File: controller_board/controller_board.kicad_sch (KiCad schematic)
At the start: 51 parts, among them IC1 LD1117-3.3V-SOT223, J3 DebugUSART (PinHeader_01x03_P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, J4 Debug GPIO (PinHeader_01x02_P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, Q1 DTC114ECA (SOT-23), Q2 DTC114ECA (SOT-23), U1 ADM3485EARZ-REEL (SOIC-8), U2 PAI141M30 (SOIC-16), U5 SMU02N-05

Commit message: DC, contr, mb, step v2
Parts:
- removed J3: DebugUSART (PinHeader_01x03_P2.54mm), Connector_PinHeader_2.54mm:PinHeader_1x03_P2.54mm_Vertical, symbol Connector:Conn_01x03_Pin
- removed J4: Debug GPIO (PinHeader_01x02_P2.54mm), Connector_PinHeader_2.54mm:PinHeader_1x02_P2.54mm_Vertical, symbol Connector:Conn_01x02_Pin
- C13, C5, C8, C9: value 0,1uF 50V 0805 -> 0,1uF 100V 0603; footprint PCM_Capacitor_SMD_AKL:C_0805_2012Metric_Pad1.18x1.45mm_HandSolder -> Capacitor_SMD:C_0603_1608Metric
- C14: value 47uF 63V D10,5 -> 47uF 63V D6,3 H11
- C2, C7: value 270 pf X7R 1206 2000v 202R18W271KW4E -> 270 pf X7R 1206 2000v 202R18W271KW4E
- IC1: footprint PCM_Package_TO_SOT_SMD_AKL:SOT-89-3_BigPads -> PCM_Package_TO_SOT_SMD_AKL:SOT-223-3_TabPin2
- U2: value PAI141M30 (SOIC-16) -> pia141M30 (SOIC-16)
- renumbered TP26 to TP1, TP27 to TP1, TP28 to TP1, TP29 to TP1, TP30 to TP1, TP32 to TP1, TP33 to TP1, TP31 to TP1, TP25 to TP1
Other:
- sheet NUCLEO-64F411 ports: added none; removed DE_USART6, GPIO1, GPIO2, RX_USART6, TX_USART6

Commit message: DC, contr, mb, digit in v2.1
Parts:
- C12: footprint PCM_Capacitor_SMD_AKL:C_0805_2012Metric_Pad1.18x1.45mm_HandSolder -> Capacitor_SMD:C_0805_2012Metric

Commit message: controller метализированные отверстия
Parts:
- H3, H4, H5: footprint MountingHole:MountingHole_3.2mm_M3 -> MountingHole:MountingHole_3.2mm_M3_DIN965_Pad
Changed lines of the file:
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@@
       (effects (font (size 1.27 1.27)) (justify left) hide)
     )
-    (property "Footprint" "MountingHole:MountingHole_3.2mm_M3" (at 137.16 185.42 0)
+    (property "Footprint" "MountingHole:MountingHole_3.2mm_M3_DIN965_Pad" (at 137.16 185.42 0)
       (effects (font (size 1.27 1.27)) hide)
     )
@@
       (effects (font (size 1.27 1.27)) (justify left) hide)
     )
-    (property "Footprint" "MountingHole:MountingHole_3.2mm_M3" (at 118.11 185.42 0)
+    (property "Footprint" "MountingHole:MountingHole_3.2mm_M3_DIN965_Pad" (at 118.11 185.42 0)
       (effects (font (size 1.27 1.27)) hide)
     )
@@
       (effects (font (size 1.27 1.27)) (justify left) hide)
     )
-    (property "Footprint" "MountingHole:MountingHole_3.2mm_M3" (at 95.25 185.42 0)
-      (effects (font (size 1.27 1.27)) hide)
-    )
+    (property "Footprint" "MountingHole:MountingHole_3.2mm_M3_DIN965_Pad" (at 95.25 185.42 0)
+      (effects (font (size 1.27 1.27)) hide)
+    )

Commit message: controller тестовые площадки
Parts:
- added TP1 (x3): TestPoint, PCM_4ms_TestPoint:TestPoint_D1, symbol Connector:TestPoint
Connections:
- net GND1: now also TP1.1
- net GNDA: now also TP1.1
- net GNDD: now also TP1.1
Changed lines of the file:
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@@
   (junction (at 237.49 123.19) (diameter 0) (color 0 0 0 0)
   )
+  (junction (at 63.5 58.42) (diameter 0) (color 0 0 0 0)
+  )
   (junction (at 165.1 109.22) (diameter 0) (color 0 0 0 0)
   )
@@
   (junction (at 31.75 184.15) (diameter 0) (color 0 0 0 0)
   )
+  (junction (at 165.1 119.38) (diameter 0) (color 0 0 0 0)
+  )
   (junction (at 120.65 20.32) (diameter 0) (color 0 0 0 0)
   )
   (junction (at 82.55 45.72) (diameter 0) (color 0 0 0 0)
+  )
+  (junction (at 246.38 119.38) (diameter 0) (color 0 0 0 0)
   )
   (junction (at 101.6 48.26) (diameter 0) (color 0 0 0 0)
@@
     (stroke (width 0) (type default))
   )
+  (wire (pts (xy 157.48 119.38) (xy 165.1 119.38))
+    (stroke (width 0) (type default))
+  )
   (wire (pts (xy 73.66 43.18) (xy 77.47 43.18))
     (stroke (width 0) (type default))
@@
     (stroke (width 0) (type default))
   )
-  (wire (pts (xy 246.38 116.84) (xy 246.38 120.65))
+  (wire (pts (xy 246.38 116.84) (xy 246.38 119.38))
     (stroke (width 0) (type default))
   )
@@
     (stroke (width 0) (type default))
   )
+  (wire (pts (xy 165.1 119.38) (xy 165.1 118.11))
+    (stroke (width 0) (type default))
+  )
   (wire (pts (xy 77.47 45.72) (xy 77.47 48.26))
     (stroke (width 0) (type default))
   )
+  (wire (pts (xy 165.1 121.92) (xy 165.1 119.38))
+    (stroke (width 0) (type default))
+  )
   (wire (pts (xy 111.76 40.64) (xy 111.76 43.18))
     (stroke (width 0) (type default))
@@
     (stroke (width 0) (type default))
   )
+  (wire (pts (xy 246.38 119.38) (xy 246.38 120.65))
+    (stroke (width 0) (type default))
+  )
   (wire (pts (xy 63.5 30.48) (xy 63.5 34.29))
     (stroke (width 0) (type default))
@@
     (stroke (width 0) (type default))
   )
+  (wire (pts (xy 63.5 58.42) (xy 63.5 60.96))
+    (stroke (width 0) (type default))
+  )
   (wire (pts (xy 237.49 147.32) (xy 241.3 147.32))
     (stroke (width 0) (type default))
@@
     (stroke (width 0) (type default))
   )
+  (wire (pts (xy 246.38 119.38) (xy 250.19 119.38))
+    (stroke (width 0) (type default))
+  )
   (wire (pts (xy 63.5 26.67) (xy 101.6 26.67))
     (stroke (width 0) (type default))
@@
     (stroke (width 0) (type default))
   )
-  (wire (pts (xy 63.5 55.88) (xy 63.5 60.96))
+  (wire (pts (xy 63.5 55.88) (xy 63.5 58.42))
     (stroke (width 0) (type default))
   )
@@
         (path "/0ad4c27f-47f6-4faf-ae8a-ed32884f7b20"
           (reference "TP27") (unit 1)
+        )
+      )
+      (project "Плата внешних шаговых двигателей"
+        (path "/7f8f7dc9-8c50-44ed-985c-35a6d8c67be0/0d239b34-7914-40bc-9b83-7e562c30defe"
+          (reference "TP22") (unit 1)
+        )
+        (path "/7f8f7dc9-8c50-44ed-985c-35a6d8c67be0/1f6eaeee-a46e-4730-b225-3a410300814a"
+          (reference "TP1") (unit 1)
+        )
+      )
+    )
+  )
+  (symbol (lib_id "Connector:TestPoint") (at 63.5 58.42 270) (unit 1)
+    (in_bom no) (on_board yes) (dnp no)
+    (property "Reference" "TP1" (at 68.58 57.15 0)
+      (effects (font (size 1.27 1.27)) (justify left))
+    )
+    (property "Value" "TestPoint" (at 65.532 60.96 0)
+      (effects (font (size 1.27 1.27)) (justify left) hide)
+    )
+    (property "Footprint" "PCM_4ms_TestPoint:TestPoint_D1" (at 63.5 63.5 0)
+      (effects (font (size 1.27 1.27)) hide)
+    )
+    (property "Datasheet" "~" (at 63.5 63.5 0)
+      (effects (font (size 1.27 1.27)) hide)
+    )
+    (pin "1")
+    (instances
+      (project "controller_board"
+        (path "/0ad4c27f-47f6-4faf-ae8a-ed32884f7b20/aa98b9ed-d882-4e12-89ef-5fad349452f5"
+          (reference "TP1") (unit 1)
+        )
+        (path "/0ad4c27f-47f6-4faf-ae8a-ed32884f7b20"
+          (reference "G1") (unit 1)
         )
       )
@@
     )
   )
-  (symbol (lib_id "PCM_4ms_Power-symbol:GNDA") (at 165.1 118.11 0) (unit 1)
-    (in_bom yes) (on_board yes) (dnp no) (fields_autoplaced)
-    (property "Reference" "#PWR05" (at 165.1 124.46 0)
-      (effects (font (size 1.27 1.27)) hide)
-    )
-    (property "Value" "GNDA" (at 165.1 123.19 0)
-      (effects (font (size 1.27 1.27)))
-    )
-    (property "Footprint" "" (at 165.1 118.11 0)
-      (effects (font (size 1.27 1.27)) hide)
-    )
-    (property "Datasheet" "" (at 165.1 118.11 0)
+  (symbol (lib_id "PCM_4ms_Power-symbol:GNDA") (at 165.1 121.92 0) (unit 1)
+    (in_bom yes) (on_board yes) (dnp no) (fields_autoplaced)
+    (property "Reference" "#PWR05" (at 165.1 128.27 0)
+      (effects (font (size 1.27 1.27)) hide)
+    )
+    (property "Value" "GNDA" (at 165.1 127 0)
+      (effects (font (size 1.27 1.27)))
+    )
+    (property "Footprint" "" (at 165.1 121.92 0)
+      (effects (font (size 1.27 1.27)) hide)
+    )
+    (property "Datasheet" "" (at 165.1 121.92 0)
       (effects (font (size 1.27 1.27)) hide)
     )
@@
     )
   )
+  (symbol (lib_id "Connector:TestPoint") (at 250.19 119.38 270) (unit 1)
+    (in_bom no) (on_board yes) (dnp no)
+    (property "Reference" "TP1" (at 255.27 118.11 0)
+      (effects (font (size 1.27 1.27)) (justify left))
+    )
+    (property "Value" "TestPoint" (at 252.222 121.92 0)
+      (effects (font (size 1.27 1.27)) (justify left) hide)
+    )
+    (property "Footprint" "PCM_4ms_TestPoint:TestPoint_D1" (at 250.19 124.46 0)
+      (effects (font (size 1.27 1.27)) hide)
+    )
+    (property "Datasheet" "~" (at 250.19 124.46 0)
+      (effects (font (size 1.27 1.27)) hide)
+    )
+    (pin "1")
+    (instances
+      (project "controller_board"
+        (path "/0ad4c27f-47f6-4faf-ae8a-ed32884f7b20/aa98b9ed-d882-4e12-89ef-5fad349452f5"
+          (reference "TP1") (unit 1)
+        )
+        (path "/0ad4c27f-47f6-4faf-ae8a-ed32884f7b20"
+          (reference "GD1") (unit 1)
+        )
+      )
+      (project "Плата внешних шаговых двигателей"
+        (path "/7f8f7dc9-8c50-44ed-985c-35a6d8c67be0/0d239b34-7914-40bc-9b83-7e562c30defe"
+          (reference "TP22") (unit 1)
+        )
+        (path "/7f8f7dc9-8c50-44ed-985c-35a6d8c67be0/1f6eaeee-a46e-4730-b225-3a410300814a"
+          (reference "TP1") (unit 1)
+        )
+      )
+    )
+  )
   (symbol (lib_id "power:GNDD") (at 100.33 93.98 0) (unit 1)
     (in_bom yes) (on_board yes) (dnp no) (fields_autoplaced)
@@
         )
       )
+    )
+  )
+  (symbol (lib_id "Connector:TestPoint") (at 157.48 119.38 90) (unit 1)
+    (in_bom no) (on_board yes) (dnp no)
+    (property "Reference" "TP1" (at 152.4 120.65 0)
+      (effects (font (size 1.27 1.27)) (justify left))
+    )
+    (property "Value" "TestPoint" (at 155.448 116.84 0)
+      (effects (font (size 1.27 1.27)) (justify left) hide)
+    )
+    (property "Footprint" "PCM_4ms_TestPoint:TestPoint_D1" (at 157.48 114.3 0)
+      (effects (font (size 1.27 1.27)) hide)
+    )
+    (property "Datasheet" "~" (at 157.48 114.3 0)
+      (effects (font (size 1.27 1.27)) hide)
+    )
+    (pin "1")
+    (instances
+      (project "controller_board"
+        (path "/0ad4c27f-47f6-4faf-ae8a-ed32884f7b20/aa98b9ed-d882-4e12-89ef-5fad349452f5"
+          (reference "TP1") (unit 1)
+        )
+        (path "/0ad4c27f-47f6-4faf-ae8a-ed32884f7b20"
+          (reference "GA1") (unit 1)
+        )
+      )
+      (project "Плата внешних шаговых двигателей"
+        (path "/7f8f7dc9-8c50-44ed-985c-35a6d8c67be0/0d239b34-7914-40bc-9b83-7e562c30defe"
+          (reference "TP22") (unit 1)
+        )
+        (path "/7f8f7dc9-8c50-44ed-985c-35a6d8c67be0/1f6eaeee-a46e-4730-b225-3a410300814a"
+          (reference "TP1") (unit 1)
+        )
+      )

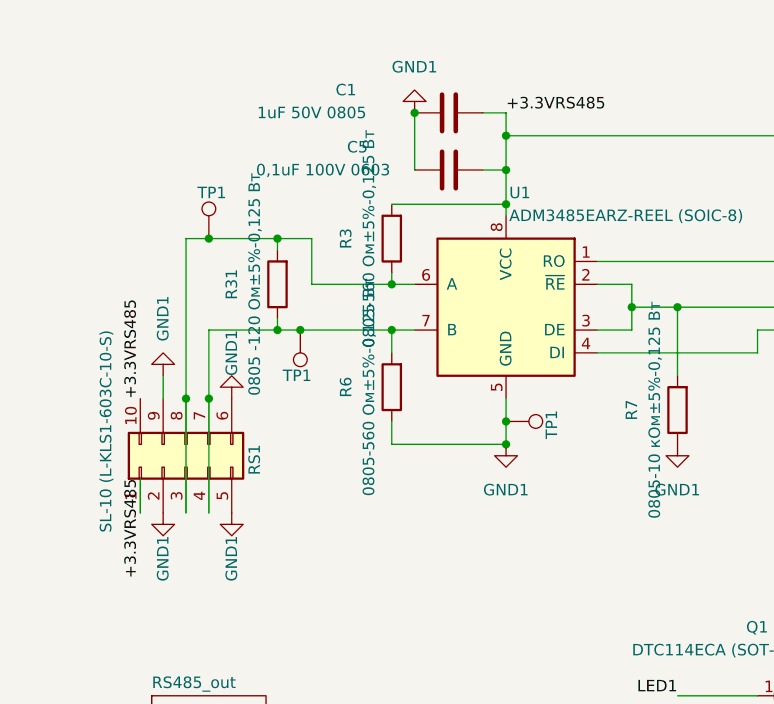
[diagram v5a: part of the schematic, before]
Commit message: all замменил резисторы failsafe в плате контроллера и обрал из перечня во всех остальных
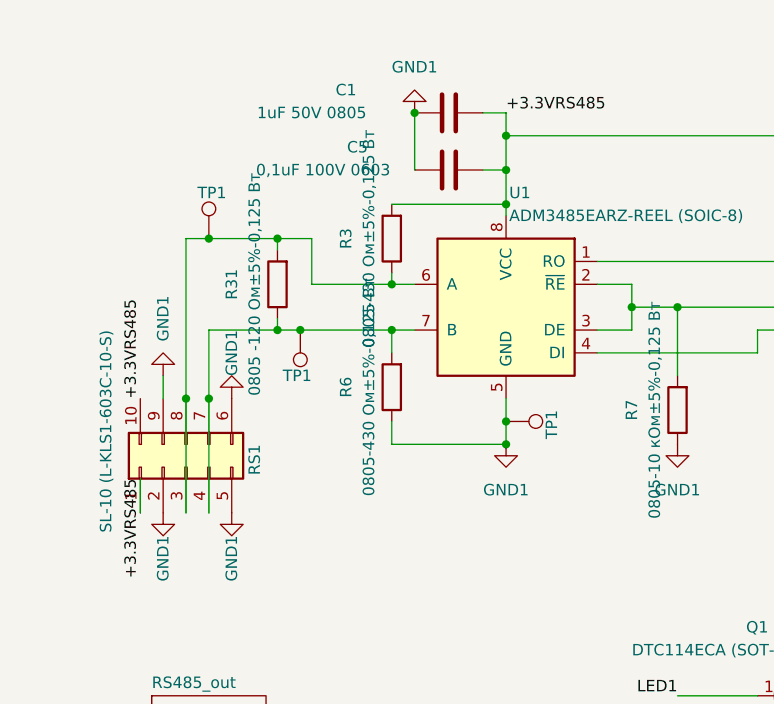
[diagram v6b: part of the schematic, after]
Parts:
- R3, R6: value 0805-560 Ом±5%-0,125 Вт -> 0805-430 Ом±5%-0,125 Вт
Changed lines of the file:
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@@
       (effects (font (size 1.27 1.27)))
     )
-    (property "Value" "0805-560 Ом±5%-0,125 Вт" (at 48.26 38.1 90)
+    (property "Value" "0805-430 Ом±5%-0,125 Вт" (at 48.26 38.1 90)
       (effects (font (size 1.27 1.27)))
     )
@@
       (effects (font (size 1.27 1.27)))
     )
-    (property "Value" "0805-560 Ом±5%-0,125 Вт" (at 48.26 54.61 90)
-      (effects (font (size 1.27 1.27)))
-    )
+    (property "Value" "0805-430 Ом±5%-0,125 Вт" (at 48.26 54.61 90)
+      (effects (font (size 1.27 1.27)))
+    )
